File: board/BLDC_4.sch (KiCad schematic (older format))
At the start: 23 parts, among them P1 Interface, P3 USB_B, P4 Power, U2 AP1117D33

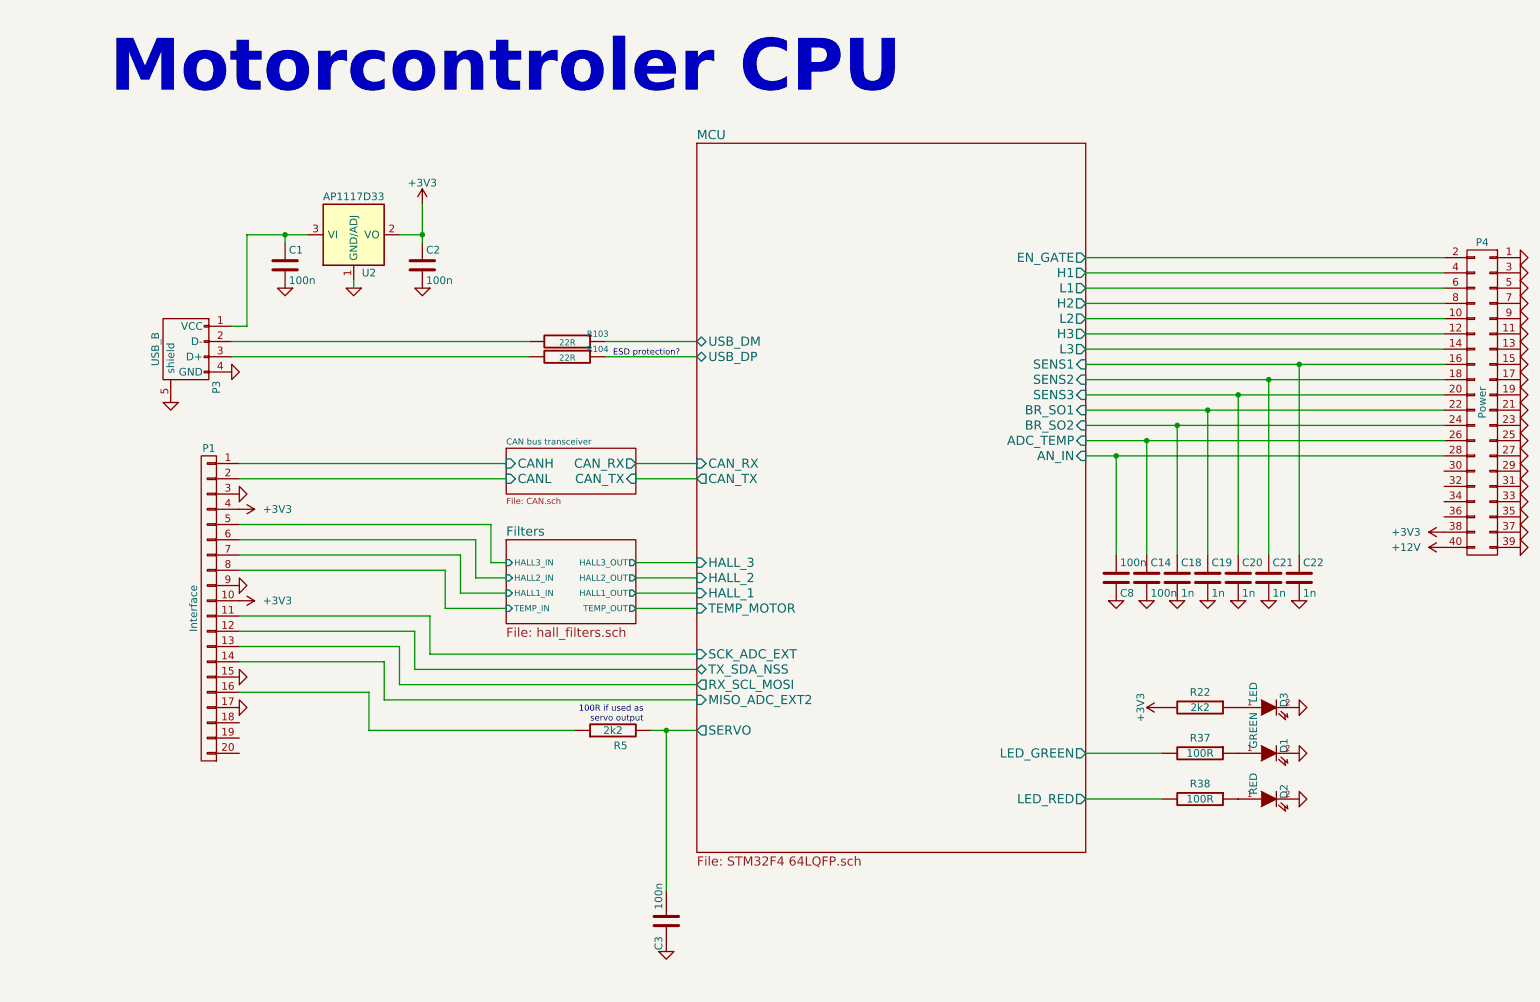
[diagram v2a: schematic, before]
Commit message: - some power supply changes
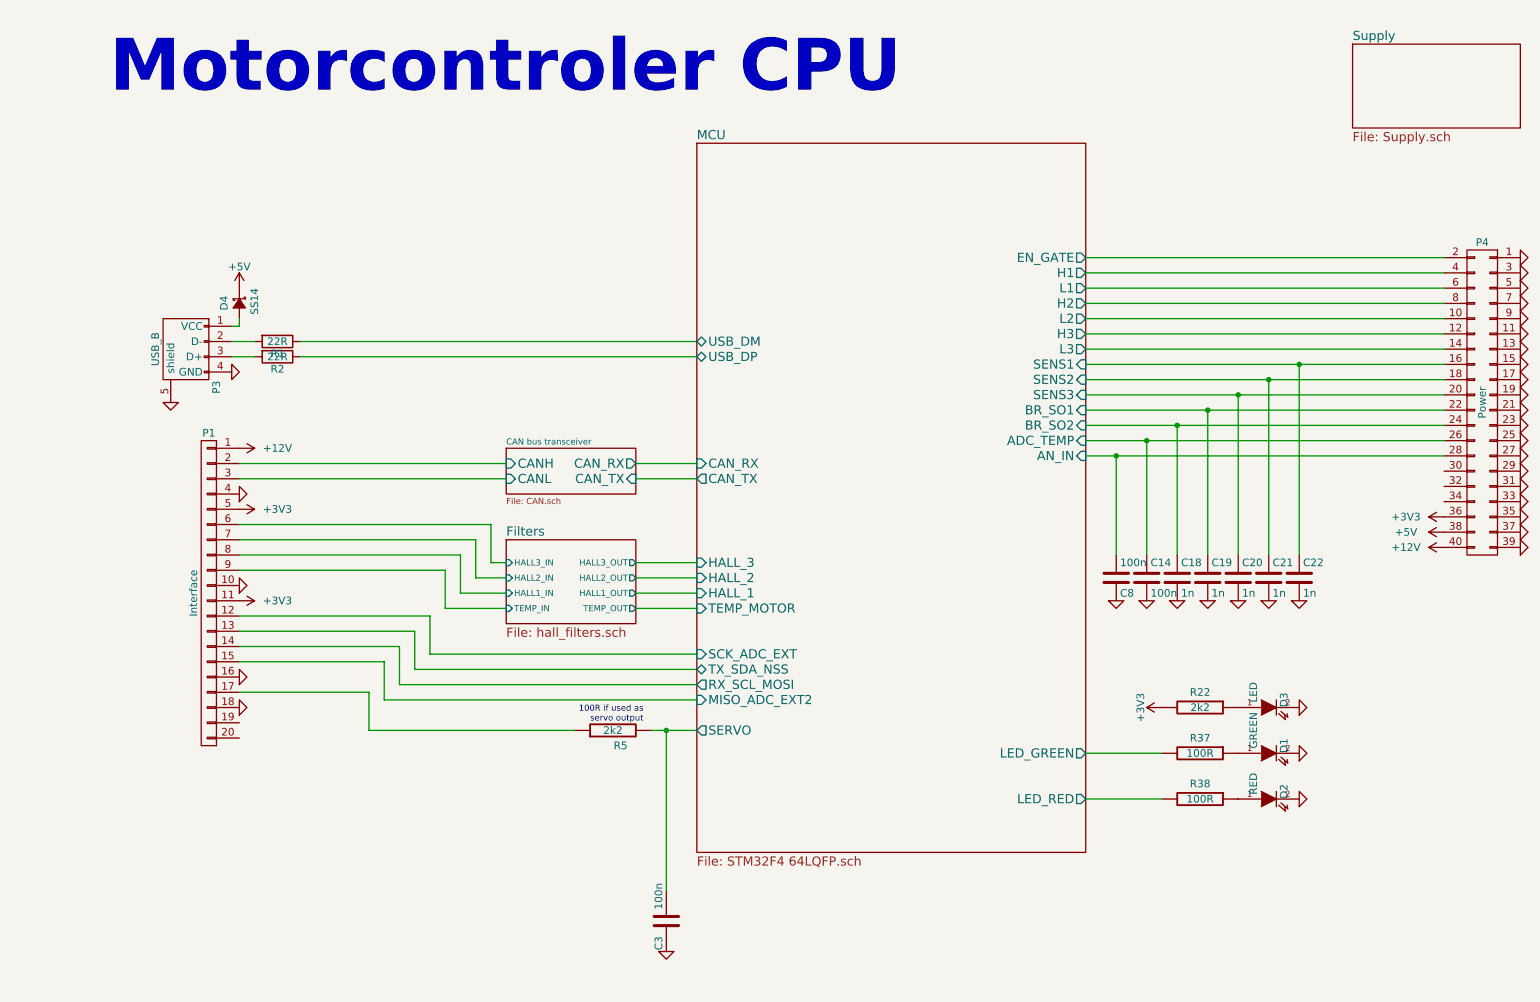
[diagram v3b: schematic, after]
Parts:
- removed C1, C2: 100n, Capacitors_SMD:C_0805, symbol C
- removed R103, R104: 22R, Resistors_SMD:R_0805, symbol R-RESCUE-BLDC_4
- removed U2: AP1117D33, TO_SOT_Packages_SMD:SOT-223, symbol AP1117D33
- added D4: SS14, Diodes_SMD:SMA_Standard, symbol D_Schottky_Small
- added R1, R2: 22R, Resistors_SMD:R_0805, symbol R
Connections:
- net +12V: now also P1.1 (P1)
- net +3V3: now also P1.11 (P11), P1.5 (P5), P4.36 (P36); no longer P1.10 (P10), P1.4 (P4), P4.38 (P38)
- net CAN bus transceiver/CANH: now also P1.2 (P2); no longer P1.1 (P1)
- net CAN bus transceiver/CANL: now also P1.3 (P3); no longer P1.2 (P2)
- net Filters/HALL1_IN: now also P1.8 (P8); no longer P1.7 (P7)
- net Filters/HALL2_IN: now also P1.7 (P7); no longer P1.6 (P6)
- net Filters/HALL3_IN: now also P1.6 (P6); no longer P1.5 (P5)
- net Filters/TEMP_IN: now also P1.9 (P9); no longer P1.8 (P8)
- net GND: now also P1.10 (P10), P1.16 (P16), P1.18 (P18), P1.4 (P4); no longer P1.15 (P15), P1.17 (P17), P1.3 (P3), P1.9 (P9)
- net MCU/MISO_ADC_EXT2: now also P1.15 (P15); no longer P1.14 (P14)
- net MCU/RX_SCL_MOSI: now also P1.14 (P14); no longer P1.13 (P13)
- net MCU/SCK_ADC_EXT: now also P1.12 (P12); no longer P1.11 (P11)
- net MCU/TX_SDA_NSS: now also P1.13 (P13); no longer P1.12 (P12)
- net MCU/USB_DM: now also R1.1
- net MCU/USB_DP: now also R2.1
- net at R5.1: now also P1.17 (P17); no longer P1.16 (P16)
- net at P3.2 (D-): now also R1.2
- net at P3.3 (D+): now also R2.2
- net at P3.1 (VCC): now also D4.2 (A)
- new net +5V: D4.1 (K), P4.38 (P38)
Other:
- note removed: "ESD protection?\n"
- moved on the sheet: P1
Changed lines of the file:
@@
 $Descr A4 11693 8268
 encoding utf-8
-Sheet 1 4
+Sheet 1 5
 Title "BLDC Driver 4.11"
 Date "21 aug 2015"
@@
 Text Notes 4650 5350 2    40   ~ 0
 100R if used as\nservo output
-Text Notes 4450 2950 0    40   ~ 0
-ESD protection?\n
 Text Notes 1150 1250 0    340  ~ 68
 Motorcontroler CPU
@@
 $EndSheet
 $Comp
-L R-RESCUE-BLDC_4 R103
-U 1 1 53FCA251
-P 4150 2850
-F 0 "R103" V 4100 3050 40  0000 C CNN
-F 1 "22R" V 4157 2851 40  0000 C CNN
-F 2 "Resistors_SMD:R_0805" V 4080 2850 30  0001 C CNN
-F 3 "" H 4150 2850 30  0000 C CNN
-	1    4150 2850
-	0    1    1    0
-$EndComp
-$Comp
-L R-RESCUE-BLDC_4 R104
-U 1 1 53FCA272
-P 4150 2950
-F 0 "R104" V 4100 3150 40  0000 C CNN
-F 1 "22R" V 4157 2951 40  0000 C CNN
-F 2 "Resistors_SMD:R_0805" V 4080 2950 30  0001 C CNN
-F 3 "" H 4150 2950 30  0000 C CNN
-	1    4150 2950
-	0    1    1    0
-$EndComp
-$Comp
 L R-RESCUE-BLDC_4 R38
 U 1 1 53FC020B
@@
 L +3V3 #PWR025
 U 1 1 57527A66
-P 9900 4100
-F 0 "#PWR025" H 9900 3950 50  0001 C CNN
-F 1 "+3V3" V 9900 4350 50  0000 C CNN
-F 2 "" H 9900 4100 50  0000 C CNN
-F 3 "" H 9900 4100 50  0000 C CNN
-	1    9900 4100
+P 9900 4000
+F 0 "#PWR025" H 9900 3850 50  0001 C CNN
+F 1 "+3V3" V 9900 4250 50  0000 C CNN
+F 2 "" H 9900 4000 50  0000 C CNN
+F 3 "" H 9900 4000 50  0000 C CNN
+	1    9900 4000
 	0    -1   -1   0
 $EndComp
@@
 L CONN_01X20 P1
 U 1 1 57528DF6
-P 1800 4600
-F 0 "P1" H 1800 5650 50  0000 C CNN
-F 1 "Interface" V 1900 4600 50  0000 C CNN
-F 2 "Pin_Headers:Pin_Header_Straight_2x10" H 1800 4600 60  0001 C CNN
-F 3 "" H 1800 4600 60  0000 C CNN
-	1    1800 4600
+P 1800 4500
+F 0 "P1" H 1800 5550 50  0000 C CNN
+F 1 "Interface" V 1900 4500 50  0000 C CNN
+F 2 "Pin_Headers:Pin_Header_Straight_2x10" H 1800 4500 60  0001 C CNN
+F 3 "" H 1800 4500 60  0000 C CNN
+	1    1800 4500
 	-1   0    0    -1
 $EndComp
@@
 $EndComp
 $Comp
-L GND-RESCUE-BLDC_4 #PWR034
-U 1 1 5754CBE4
-P 2750 2500
-F 0 "#PWR034" H 2750 2500 30  0001 C CNN
-F 1 "GND" H 2750 2430 30  0001 C CNN
-F 2 "" H 2750 2500 60  0001 C CNN
-F 3 "" H 2750 2500 60  0001 C CNN
-	1    2750 2500
-	-1   0    0    -1
-$EndComp
-$Comp
-L GND-RESCUE-BLDC_4 #PWR035
-U 1 1 5754CD1B
-P 2300 2500
-F 0 "#PWR035" H 2300 2500 30  0001 C CNN
-F 1 "GND" H 2300 2430 30  0001 C CNN
-F 2 "" H 2300 2500 60  0001 C CNN
-F 3 "" H 2300 2500 60  0001 C CNN
-	1    2300 2500
-	-1   0    0    -1
-$EndComp
-$Comp
-L GND-RESCUE-BLDC_4 #PWR036
-U 1 1 5754DB03
-P 3200 2500
-F 0 "#PWR036" H 3200 2500 30  0001 C CNN
-F 1 "GND" H 3200 2430 30  0001 C CNN
-F 2 "" H 3200 2500 60  0001 C CNN
-F 3 "" H 3200 2500 60  0001 C CNN
-	1    3200 2500
-	-1   0    0    -1
-$EndComp
-$Comp
-L +3V3 #PWR037
-U 1 1 57551927
-P 3200 1950
-F 0 "#PWR037" H 3200 1800 50  0001 C CNN
-F 1 "+3V3" H 3200 2090 50  0000 C CNN
-F 2 "" H 3200 1950 60  0000 C CNN
-F 3 "" H 3200 1950 60  0000 C CNN
-	1    3200 1950
-	1    0    0    -1
-$EndComp
-$Comp
-L C C2
-U 1 1 57553D65
-P 3200 2350
-F 0 "C2" H 3225 2450 50  0000 L CNN
-F 1 "100n" H 3225 2250 50  0000 L CNN
-F 2 "Capacitors_SMD:C_0805" H 3238 2200 30  0001 C CNN
-F 3 "" H 3200 2350 60  0000 C CNN
-	1    3200 2350
-	1    0    0    -1
-$EndComp
-$Comp
-L AP1117D33 U2
-U 1 1 57549DA9
-P 2750 2150
-F 0 "U2" H 2850 1900 50  0000 C CNN
-F 1 "AP1117D33" H 2750 2400 50  0000 C CNN
-F 2 "TO_SOT_Packages_SMD:SOT-223" H 2750 2150 60  0001 C CNN
-F 3 "" H 2750 2150 60  0000 C CNN
-	1    2750 2150
-	1    0    0    -1
-$EndComp
-$Comp
-L C C1
-U 1 1 57554BAB
-P 2300 2350
-F 0 "C1" H 2325 2450 50  0000 L CNN
-F 1 "100n" H 2325 2250 50  0000 L CNN
-F 2 "Capacitors_SMD:C_0805" H 2338 2200 30  0001 C CNN
-F 3 "" H 2300 2350 60  0000 C CNN
-	1    2300 2350
-	1    0    0    -1
-$EndComp
-$Comp
 L USB_B P3
 U 1 1 5755AD68
@@
 $EndComp
 $Comp
-L GND-RESCUE-BLDC_4 #PWR038
+L GND-RESCUE-BLDC_4 #PWR034
 U 1 1 5755CD59
 P 1950 3050
-F 0 "#PWR038" H 1950 3050 30  0001 C CNN
+F 0 "#PWR034" H 1950 3050 30  0001 C CNN
 F 1 "GND" H 1950 2980 30  0001 C CNN
 F 2 "" H 1950 3050 60  0001 C CNN
@@
 $EndComp
 $Comp
-L GND-RESCUE-BLDC_4 #PWR039
+L GND-RESCUE-BLDC_4 #PWR035
 U 1 1 5755CE93
 P 1550 3250
-F 0 "#PWR039" H 1550 3250 30  0001 C CNN
+F 0 "#PWR035" H 1550 3250 30  0001 C CNN
 F 1 "GND" H 1550 3180 30  0001 C CNN
 F 2 "" H 1550 3250 60  0001 C CNN
@@
 	5000 3750 4600 3750
 Wire Wire Line
-	3900 2850 1950 2850
+	1950 2850 2100 2850
 Wire Wire Line
-	1950 2950 3900 2950
+	1950 2950 2100 2950
 Wire Wire Line
-	4400 2850 5000 2850
+	2400 2850 5000 2850
 Wire Wire Line
-	4400 2950 5000 2950
+	2400 2950 5000 2950
 Wire Wire Line
 	8550 5850 8550 5850
@@
 	8050 5550 7550 5550
 Wire Wire Line
-	1950 2750 2050 2750
-Wire Wire Line
-	2050 2750 2050 2150
-Wire Wire Line
-	2750 2500 2750 2450
-Wire Wire Line
-	3200 1950 3200 2200
-Wire Wire Line
-	3050 2150 3200 2150
-Connection ~ 3200 2150
-Wire Wire Line
-	2050 2150 2450 2150
-Wire Wire Line
-	2300 2150 2300 2150
-Connection ~ 2300 2150
-Wire Wire Line
-	2300 2200 2300 2150
-Wire Wire Line
 	4800 6450 4800 5400
 Wire Wire Line
@@
 $EndComp
 $Comp
-L GND-RESCUE-BLDC_4 #PWR040
+L GND-RESCUE-BLDC_4 #PWR036
 U 1 1 5757A76E
 P 7750 4550
-F 0 "#PWR040" H 7750 4550 30  0001 C CNN
+F 0 "#PWR036" H 7750 4550 30  0001 C CNN
 F 1 "GND" H 7750 4480 30  0001 C CNN
 F 2 "" H 7750 4550 60  0001 C CNN
@@
 $EndComp
 $Comp
-L GND-RESCUE-BLDC_4 #PWR041
+L GND-RESCUE-BLDC_4 #PWR037
 U 1 1 5757B5DF
 P 7950 4550
-F 0 "#PWR041" H 7950 4550 30  0001 C CNN
+F 0 "#PWR037" H 7950 4550 30  0001 C CNN
 F 1 "GND" H 7950 4480 30  0001 C CNN
 F 2 "" H 7950 4550 60  0001 C CNN
@@
 $EndComp
 $Comp
-L GND-RESCUE-BLDC_4 #PWR042
+L GND-RESCUE-BLDC_4 #PWR038
 U 1 1 5757B722
 P 8150 4550
-F 0 "#PWR042" H 8150 4550 30  0001 C CNN
+F 0 "#PWR038" H 8150 4550 30  0001 C CNN
 F 1 "GND" H 8150 4480 30  0001 C CNN
 F 2 "" H 8150 4550 60  0001 C CNN
@@
 $EndComp
 $Comp
-L GND-RESCUE-BLDC_4 #PWR043
+L GND-RESCUE-BLDC_4 #PWR039
 U 1 1 5757C875
 P 8350 4550
-F 0 "#PWR043" H 8350 4550 30  0001 C CNN
+F 0 "#PWR039" H 8350 4550 30  0001 C CNN
 F 1 "GND" H 8350 4480 30  0001 C CNN
 F 2 "" H 8350 4550 60  0001 C CNN
@@
 $EndComp
 $Comp
-L GND-RESCUE-BLDC_4 #PWR044
+L GND-RESCUE-BLDC_4 #PWR040
 U 1 1 5757FA73
 P 8550 4550
-F 0 "#PWR044" H 8550 4550 30  0001 C CNN
+F 0 "#PWR040" H 8550 4550 30  0001 C CNN
 F 1 "GND" H 8550 4480 30  0001 C CNN
 F 2 "" H 8550 4550 60  0001 C CNN
@@
 $EndComp
 $Comp
-L GND-RESCUE-BLDC_4 #PWR045
+L GND-RESCUE-BLDC_4 #PWR041
 U 1 1 5757FA7F
 P 8750 4550
-F 0 "#PWR045" H 8750 4550 30  0001 C CNN
+F 0 "#PWR041" H 8750 4550 30  0001 C CNN
 F 1 "GND" H 8750 4480 30  0001 C CNN
 F 2 "" H 8750 4550 60  0001 C CNN
@@
 $EndComp
 $Comp
-L GND-RESCUE-BLDC_4 #PWR046
+L GND-RESCUE-BLDC_4 #PWR042
 U 1 1 5757FA8B
 P 8950 4550
-F 0 "#PWR046" H 8950 4550 30  0001 C CNN
+F 0 "#PWR042" H 8950 4550 30  0001 C CNN
 F 1 "GND" H 8950 4480 30  0001 C CNN
 F 2 "" H 8950 4550 60  0001 C CNN
@@
 	8950 4250 8950 3000
 Connection ~ 8950 3000
+$Comp
+L +12V #PWR043
+U 1 1 57574636
+P 2000 3550
+F 0 "#PWR043" H 2000 3400 50  0001 C CNN
+F 1 "+12V" V 2000 3800 50  0000 C CNN
+F 2 "" H 2000 3550 50  0000 C CNN
+F 3 "" H 2000 3550 50  0000 C CNN
+	1    2000 3550
+	0    1    1    0
+$EndComp
+$Sheet
+S 9300 900  1100 550
+U 5757B5E7
+F0 "Supply" 60
+F1 "Supply.sch" 60
+$EndSheet
+$Comp
+L D_Schottky_Small D4
+U 1 1 575811AA
+P 2000 2600
+F 0 "D4" H 1950 2500 50  0000 L CNN
+F 1 "SS14" H 1900 2700 50  0000 L CNN
+F 2 "Diodes_SMD:SMA_Standard" V 2000 2600 60  0001 C CNN
+F 3 "" V 2000 2600 60  0000 C CNN
+	1    2000 2600
+	0    1    1    0
+$EndComp
+$Comp
+L +5V #PWR044
+U 1 1 575812F1
+P 2000 2500
+F 0 "#PWR044" H 2000 2350 50  0001 C CNN
+F 1 "+5V" H 2000 2640 50  0000 C CNN
+F 2 "" H 2000 2500 60  0000 C CNN
+F 3 "" H 2000 2500 60  0000 C CNN
+	1    2000 2500
+	1    0    0    -1
+$EndComp
+$Comp
+L R R1
+U 1 1 57581E88
+P 2250 2850
+F 0 "R1" V 2330 2850 50  0000 C CNN
+F 1 "22R" V 2250 2850 50  0000 C CNN
+F 2 "Resistors_SMD:R_0805" V 2180 2850 30  0001 C CNN
+F 3 "" H 2250 2850 30  0000 C CNN
+	1    2250 2850
+	0    1    1    0
+$EndComp
+$Comp
+L R R2
+U 1 1 57582148
+P 2250 2950
+F 0 "R2" V 2330 2950 50  0000 C CNN
+F 1 "22R" V 2250 2950 50  0000 C CNN
+F 2 "Resistors_SMD:R_0805" V 2180 2950 30  0001 C CNN
+F 3 "" H 2250 2950 30  0000 C CNN
+	1    2250 2950
+	0    1    1    0
+$EndComp
+Wire Wire Line
+	2000 2700 2000 2750
+Wire Wire Line
+	2000 2750 1950 2750
+$Comp
+L +5V #PWR045
+U 1 1 5758912C
+P 9900 4100
+F 0 "#PWR045" H 9900 3950 50  0001 C CNN
+F 1 "+5V" V 9900 4350 50  0000 C CNN
+F 2 "" H 9900 4100 60  0000 C CNN
+F 3 "" H 9900 4100 60  0000 C CNN
+	1    9900 4100
+	0    -1   -1   0
+$EndComp
 $EndSCHEMATC

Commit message: - updated layout with recent changes in schematic
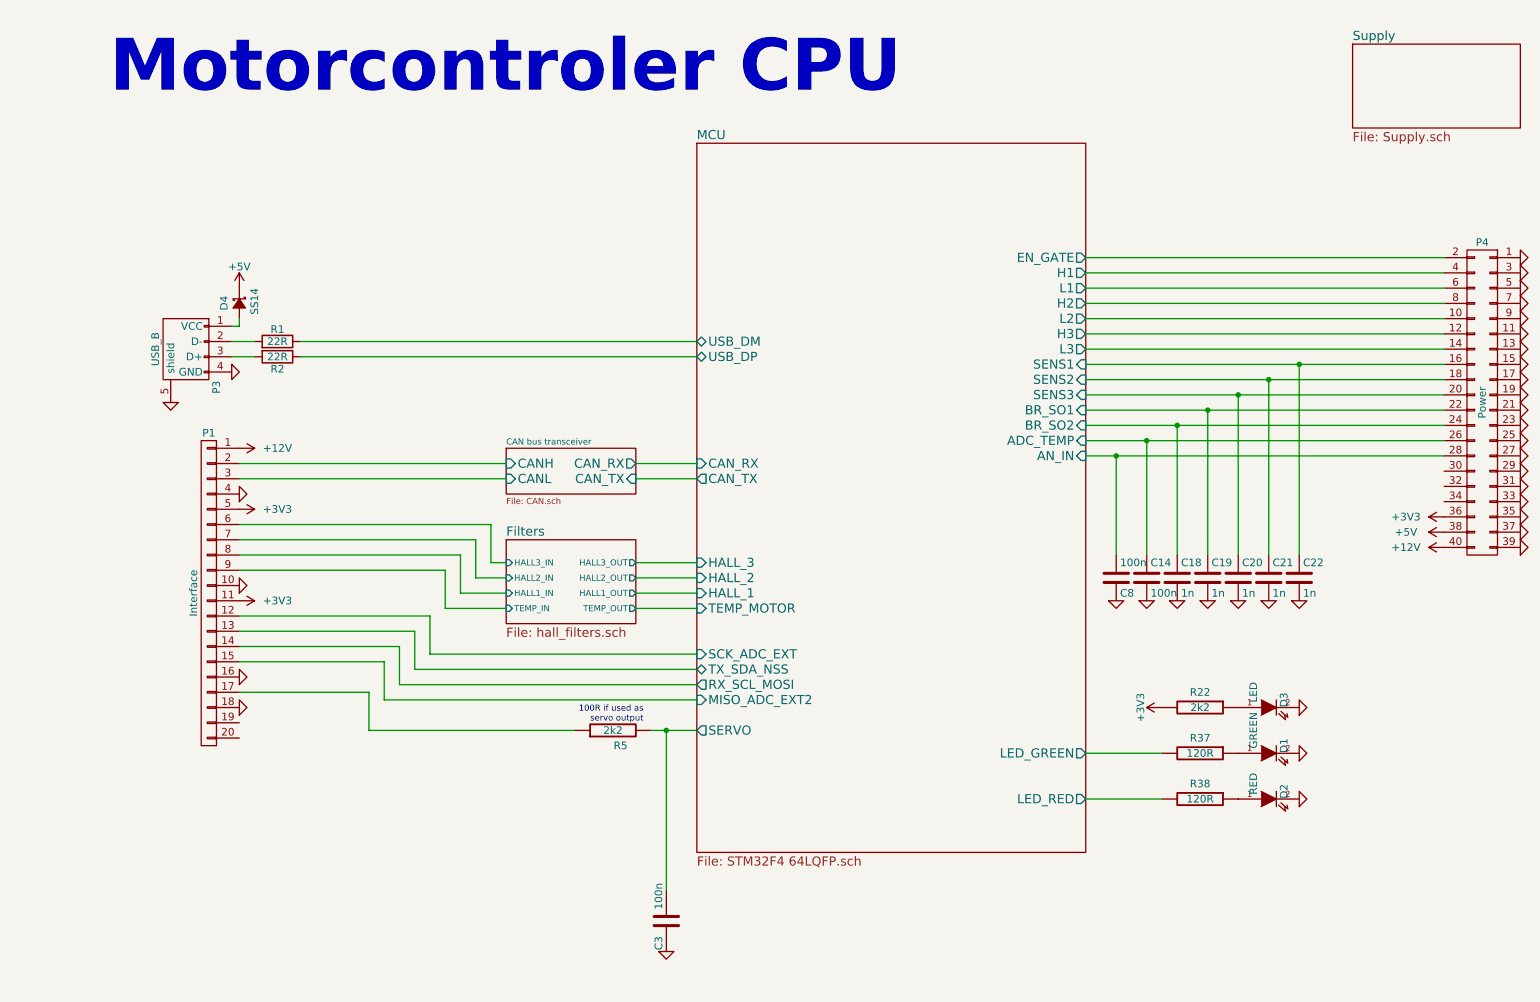
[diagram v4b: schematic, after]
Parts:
- P1: footprint Pin_Headers:Pin_Header_Straight_2x10 -> alexmod:XG4A_20
- P4: footprint Pin_Headers:Pin_Header_Straight_2x20 -> alexmod:XG4A_40
- R37, R38: value 100R -> 120R
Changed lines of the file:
@@
 P 8300 5850
 F 0 "R38" V 8200 5850 50  0000 C CNN
-F 1 "100R" V 8300 5850 50  0000 C CNN
+F 1 "120R" V 8300 5850 50  0000 C CNN
 F 2 "Resistors_SMD:R_0805" H 8300 5850 60  0001 C CNN
 F 3 "" H 8300 5850 60  0001 C CNN
@@
 P 8300 5550
 F 0 "R37" V 8200 5550 50  0000 C CNN
-F 1 "100R" V 8300 5550 50  0000 C CNN
+F 1 "120R" V 8300 5550 50  0000 C CNN
 F 2 "Resistors_SMD:R_0805" H 8300 5550 60  0001 C CNN
 F 3 "" H 8300 5550 60  0001 C CNN
@@
 F 0 "P4" H 10150 4300 50  0000 C CNN
 F 1 "Power" V 10150 3250 50  0000 C CNN
-F 2 "Pin_Headers:Pin_Header_Straight_2x20" H 10150 2300 50  0001 C CNN
+F 2 "alexmod:XG4A_40" H 10150 2300 50  0001 C CNN
 F 3 "" H 10150 2300 50  0000 C CNN
 	1    10150 3250
@@
 F 0 "P1" H 1800 5550 50  0000 C CNN
 F 1 "Interface" V 1900 4500 50  0000 C CNN
-F 2 "Pin_Headers:Pin_Header_Straight_2x10" H 1800 4500 60  0001 C CNN
+F 2 "alexmod:XG4A_20" H 1800 4500 60  0001 C CNN
 F 3 "" H 1800 4500 60  0000 C CNN
 	1    1800 4500
@@
 F 3 "" H 2250 2850 30  0000 C CNN
 	1    2250 2850
-	0    1    1    0
+	0    1    -1   0
 $EndComp
 $Comp
